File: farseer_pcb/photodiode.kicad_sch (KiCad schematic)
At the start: 6 parts, among them J3 UMC_JACK_SMD, U4 OPA381

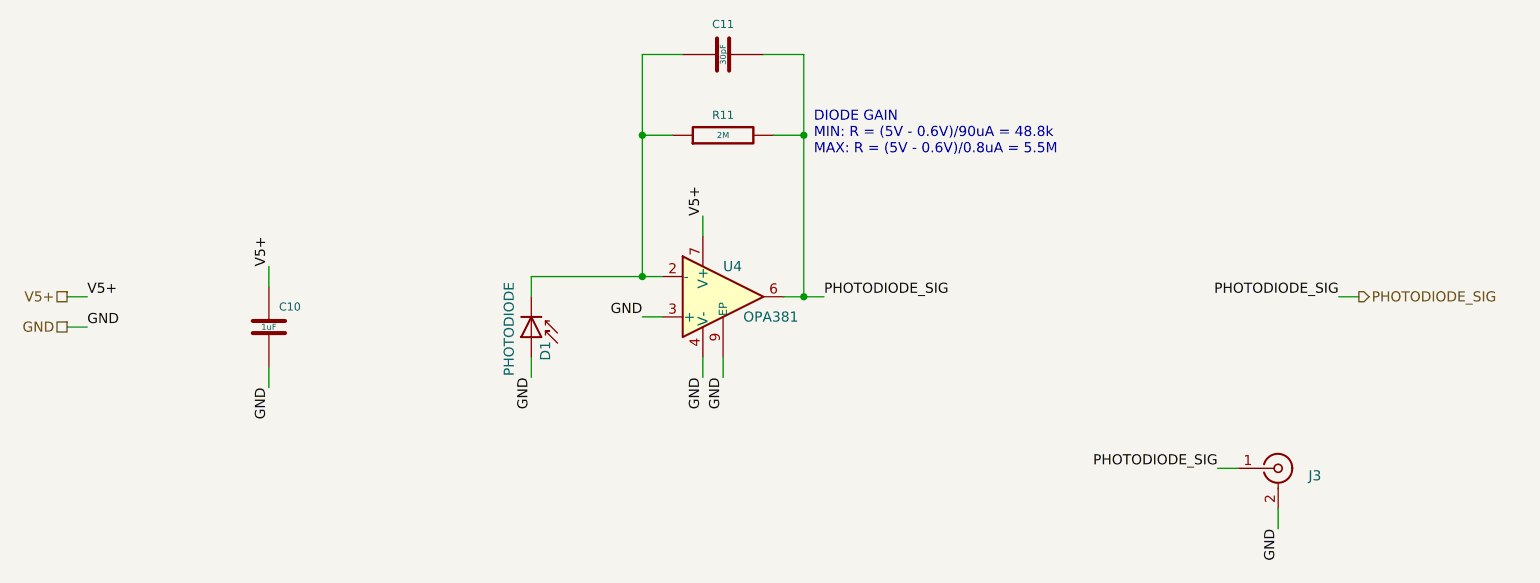
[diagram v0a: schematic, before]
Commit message: Begin board resize
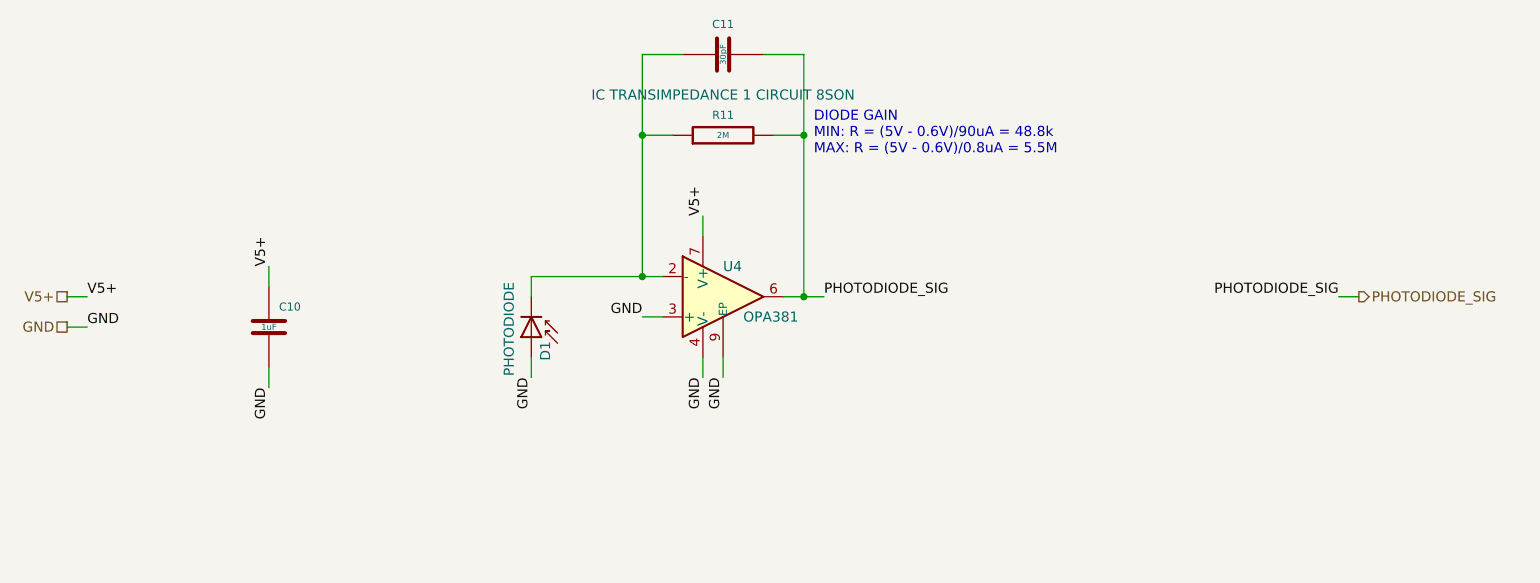
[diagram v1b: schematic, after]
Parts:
- removed J3: UMC_JACK_SMD, Janelia:UMC_AMPHENOL_A-1JB, symbol Janelia:CONN_UMC_JACK_SMD
- C10: LCSC (none) -> C307413; MFN Samsung Electro-Mechanics -> (none); MPN CL05A105KL5NRNC -> (none); Manufacturer (none) -> Samsung Electro-Mechanics; Manufacturer Part Number (none) -> CL05A105KL5NRNC; Synopsis (none) -> CAP CER 1UF 35V X5R
- C11: MFN KEMET -> (none); MPN C0402C300J5GACAUTO -> (none); Manufacturer (none) -> KEMET; Manufacturer Part Number (none) -> C0402C300J5GACAUTO; Synopsis (none) -> CAP CER 30PF 50V C0G/NP0
- D1: MFN American Bright Optoelectronics Corporation -> (none); MPN BPD-BQDA38V-FZ04 -> (none); Manufacturer (none) -> American Bright Optoelectronics Corporation; Manufacturer Part Number (none) -> BPD-BQDA38V-FZ04; Synopsis (none) -> SENSOR PHOTODIODE RADIAL
- R11: MFN Panasonic Electronic Components -> (none); MPN ERJ-PM8F2004V -> (none); Manufacturer (none) -> Panasonic Electronic Components; Manufacturer Part Number (none) -> ERJ-PM8F2004V; Synopsis (none) -> RES 2.0M OHM 1% 0.66W
- U4: MFN Texas Instruments -> (none); MPN OPA381AIDRBT -> (none); Manufacturer (none) -> Texas Instruments; Manufacturer Part Number (none) -> OPA381AIDRBT; Synopsis (none) -> IC TRANSIMPEDANCE 1 CIRCUIT 8SON
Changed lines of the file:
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@@
-	(wire
-		(pts
-			(xy 203.2 106.68) (xy 200.66 106.68)
-		)
-		(stroke
-			(width 0)
-			(type default)
-		)
-	)
 	(wire
 		(pts
@@
 		(pts
 			(xy 128.27 54.61) (xy 128.27 64.77)
-		)
-		(stroke
-			(width 0)
-			(type default)
-		)
-	)
-	(wire
-		(pts
-			(xy 208.28 111.76) (xy 208.28 114.3)
 		)
 		(stroke
@@
 	)
 	(label "GND"
-		(at 208.28 114.3 270)
-		(effects
-			(font
-				(size 1.27 1.27)
-			)
-			(justify right bottom)
-		)
-	)
-	(label "GND"
 		(at 114.3 95.25 270)
 		(effects
@@
 			)
 			(justify left bottom)
-		)
-	)
-	(label "PHOTODIODE_SIG"
-		(at 200.66 106.68 180)
-		(effects
-			(font
-				(size 1.27 1.27)
-			)
-			(justify right bottom)
 		)
 	)
@@
 			)
 		)
-		(property "Description" "RES 2.0M OHM 1% 0.66W"
-			(at 130.81 55.118 90)
-			(effects
-				(font
-					(size 1.524 1.524)
+		(property "Description" ""
+			(at 138.43 64.77 0)
+			(effects
+				(font
+					(size 1.27 1.27)
 				)
 				(hide yes)
@@
 			)
 		)
-		(property "MFN" "Panasonic Electronic Components"
+		(property "Synopsis" "RES 2.0M OHM 1% 0.66W"
+			(at 130.81 55.118 90)
+			(effects
+				(font
+					(size 1.524 1.524)
+				)
+				(hide yes)
+			)
+		)
+		(property "Manufacturer" "Panasonic Electronic Components"
 			(at 138.43 64.77 0)
 			(effects
@@
 			)
 		)
-		(property "MPN" "ERJ-PM8F2004V"
+		(property "Manufacturer Part Number" "ERJ-PM8F2004V"
 			(at 138.43 64.77 0)
 			(effects
@@
 		(at 138.43 85.09 0)
 		(unit 1)
-		(exclude_from_sim no)
+		(exclude_from_sim yes)
 		(in_bom yes)
 		(on_board yes)
@@
 			)
 		)
-		(property "Description" "IC TRANSIMPEDANCE 1 CIRCUIT 8SON"
-			(at 138.43 59.69 0)
-			(effects
-				(font
-					(size 1.27 1.27)
-				)
-				(hide yes)
-			)
-		)
-		(property "MFN" "Texas Instruments"
-			(at 138.43 57.15 0)
-			(effects
-				(font
-					(size 1.27 1.27)
-				)
-				(hide yes)
-			)
-		)
-		(property "MPN" "OPA381AIDRBT"
-			(at 138.43 52.07 0)
+		(property "Description" "2.7 GHz, High-Voltage, FET-Input, Low Noise, Operational Amplifier, WSON-8"
+			(at 138.43 85.09 0)
 			(effects
 				(font
@@
 				)
 				(hide yes)
+			)
+		)
+		(property "Manufacturer" "Texas Instruments"
+			(at 138.43 57.15 0)
+			(effects
+				(font
+					(size 1.27 1.27)
+				)
+				(hide yes)
+			)
+		)
+		(property "Manufacturer Part Number" "OPA381AIDRBT"
+			(at 138.43 52.07 0)
+			(effects
+				(font
+					(size 1.27 1.27)
+				)
+				(hide yes)
+			)
+		)
+		(property "Synopsis" "IC TRANSIMPEDANCE 1 CIRCUIT 8SON"
+			(at 138.43 59.69 0)
+			(effects
+				(font
+					(size 1.27 1.27)
+				)
 			)
 		)
@@
 	)
 	(symbol
-		(lib_id "Janelia:CONN_UMC_JACK_SMD")
-		(at 208.28 106.68 0)
-		(unit 1)
-		(exclude_from_sim no)
-		(in_bom yes)
-		(on_board yes)
-		(dnp no)
-		(fields_autoplaced yes)
-		(property "Reference" "J3"
-			(at 212.09 107.6082 0)
-			(effects
-				(font
-					(size 1.27 1.27)
-				)
-				(justify left)
-			)
-		)
-		(property "Value" "UMC_JACK_SMD"
-			(at 211.201 106.68 90)
-			(effects
-				(font
-					(size 1.27 1.27)
-				)
-				(hide yes)
-			)
-		)
-		(property "Footprint" "Janelia:UMC_AMPHENOL_A-1JB"
-			(at 208.28 93.98 0)
-			(effects
-				(font
-					(size 1.27 1.27)
-				)
-				(hide yes)
-			)
-		)
-		(property "Datasheet" ""
-			(at 208.28 106.68 0)
-			(effects
-				(font
-					(size 1.27 1.27)
-				)
-				(hide yes)
-			)
-		)
-		(property "Description" "CONN UMC JACK STR 50 OHM SMD"
-			(at 208.28 91.44 0)
-			(effects
-				(font
-					(size 1.27 1.27)
-				)
-				(hide yes)
-			)
-		)
-		(property "MFN" "Amphenol RF"
-			(at 208.28 96.52 0)
-			(effects
-				(font
-					(size 1.27 1.27)
-				)
-				(hide yes)
-			)
-		)
-		(property "MPN" "A-1JB"
-			(at 208.28 121.92 0)
-			(effects
-				(font
-					(size 1.27 1.27)
-				)
-				(hide yes)
-			)
-		)
-		(property "Vendor" "Digi-Key"
-			(at 208.28 124.46 0)
-			(effects
-				(font
-					(size 1.27 1.27)
-				)
-				(hide yes)
-			)
-		)
-		(property "Vendor Part Number" "115-A-1JBCT-ND"
-			(at 208.28 119.38 0)
-			(effects
-				(font
-					(size 1.27 1.27)
-				)
-				(hide yes)
-			)
-		)
-		(pin "1"
-		)
-		(pin "2"
-		)
-		(instances
-			(project "farseer_pcb"
-				(path "/cc457ebc-4af6-4663-b19f-8cb38f061cb4/6f9841bf-b0ef-48ff-bf2c-2bd611c72bf3"
-					(reference "J3")
-					(unit 1)
-				)
-			)
-		)
-	)
-	(symbol
 		(lib_id "Janelia:PHOTODIODE_940nm_RADIAL_RA_SMD_BRIGHT")
 		(at 114.3 90.17 270)
 		(unit 1)
-		(exclude_from_sim no)
+		(exclude_from_sim yes)
 		(in_bom yes)
 		(on_board yes)
@@
 			)
 		)
-		(property "Description" "SENSOR PHOTODIODE RADIAL"
-			(at 124.46 90.17 0)
-			(effects
-				(font
-					(size 1.27 1.27)
-				)
-				(hide yes)
-			)
-		)
-		(property "MFN" "American Bright Optoelectronics Corporation"
-			(at 129.54 90.17 0)
-			(effects
-				(font
-					(size 1.27 1.27)
-				)
-				(hide yes)
-			)
-		)
-		(property "MPN" "BPD-BQDA38V-FZ04"
-			(at 121.92 90.17 0)
+		(property "Description" "Photodiode"
+			(at 114.3 90.17 0)
 			(effects
 				(font
@@
 		(property "Vendor Part Number" "BPD-BQDA38V-FZ04CT-ND"
 			(at 119.38 90.17 0)
+			(effects
+				(font
+					(size 1.27 1.27)
+				)
+				(hide yes)
+			)
+		)
+		(property "Manufacturer" "American Bright Optoelectronics Corporation"
+			(at 129.54 90.17 0)
+			(effects
+				(font
+					(size 1.27 1.27)
+				)
+				(hide yes)
+			)
+		)
+		(property "Manufacturer Part Number" "BPD-BQDA38V-FZ04"
+			(at 121.92 90.17 0)
+			(effects
+				(font
+					(size 1.27 1.27)
+				)
+				(hide yes)
+			)
+		)
+		(property "Synopsis" "SENSOR PHOTODIODE RADIAL"
+			(at 124.46 90.17 0)
 			(effects
 				(font
@@
 			)
 		)
-		(property "Description" "CAP CER 1UF 35V X5R"
-			(at 88.9 78.74 0)
-			(effects
-				(font
-					(size 1.524 1.524)
+		(property "Description" "1 µF ±10% 35V Ceramic Capacitor X5R 0402 (1005 Metric)"
+			(at 81.28 88.9 0)
+			(effects
+				(font
+					(size 1.27 1.27)
 				)
 				(hide yes)
@@
 			)
 		)
-		(property "MFN" "Samsung Electro-Mechanics"
+		(property "Synopsis" "CAP CER 1UF 35V X5R"
+			(at 88.9 78.74 0)
+			(effects
+				(font
+					(size 1.524 1.524)
+				)
+				(hide yes)
+			)
+		)
+		(property "Manufacturer" "Samsung Electro-Mechanics"
 			(at 81.28 88.9 0)
 			(effects
@@
 			)
 		)
-		(property "MPN" "CL05A105KL5NRNC"
+		(property "Manufacturer Part Number" "CL05A105KL5NRNC"
+			(at 81.28 88.9 0)
+			(effects
+				(font
+					(size 1.27 1.27)
+				)
+				(hide yes)
+			)
+		)
+		(property "LCSC" "C307413"
 			(at 81.28 88.9 0)
 			(effects
@@
 			)
 		)
-		(property "Description" "CAP CER 30PF 50V C0G/NP0"
-			(at 128.27 46.99 0)
-			(effects
-				(font
-					(size 1.524 1.524)
+		(property "Description" ""
+			(at 138.43 54.61 0)
+			(effects
+				(font
+					(size 1.27 1.27)
 				)
 				(hide yes)
@@
 			)
 		)
-		(property "MFN" "KEMET"
+		(property "Synopsis" "CAP CER 30PF 50V C0G/NP0"
+			(at 128.27 46.99 0)
+			(effects
+				(font
+					(size 1.524 1.524)
+				)
+				(hide yes)
+			)
+		)
+		(property "Manufacturer" "KEMET"
 			(at 138.43 54.61 0)
 			(effects
@@
 			)
 		)
-		(property "MPN" "C0402C300J5GACAUTO"
+		(property "Manufacturer Part Number" "C0402C300J5GACAUTO"
 			(at 138.43 54.61 0)
 			(effects
